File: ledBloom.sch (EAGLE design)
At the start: 4 parts, among them J1 455-1750-1-ND, J2 455-1750-1-ND, U1 WS2812

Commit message: adding production files
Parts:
- removed U1: WS2812, SparkFun-LED:WS2812"
- added D1: WS2812B, SparkFun-LED:WS2812B
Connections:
- net DI: now also D1.DI; no longer U1.DI
- net DO: now also D1.DO; no longer U1.DO
- net GND: now also D1.VSS; no longer U1.VSS
- net VCC: now also D1.VDD; no longer U1.VDD
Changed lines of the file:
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@@
 <?xml version="1.0" encoding="utf-8"?>
 <!DOCTYPE eagle SYSTEM "eagle.dtd">
-<eagle version="7.7.0">
+<eagle version="8.7.0">
 <drawing>
 <settings>
 <setting alwaysvectorfont="no"/>
+<setting keepoldvectorfont="yes"/>
 <setting verticaltext="up"/>
 </settings>
@@
 </classes>
 <parts>
-<part name="U1" library="SparkFun-LED" deviceset="WS2812" device="&quot;" value="WS2812"/>
 <part name="C1" library="SparkFun-Capacitors" deviceset="0.1UF" device="-0603-25V-(+80/-20%)" value="0.1uF"/>
 <part name="J1" library="SparkFun-Connectors" deviceset="CONN_03" device="" value="455-1750-1-ND"/>
@@
 <part name="GND3" library="SparkFun-PowerSymbols" deviceset="GND" device=""/>
 <part name="GND4" library="SparkFun-PowerSymbols" deviceset="GND" device=""/>
+<part name="D1" library="SparkFun-LED" deviceset="WS2812B" device="" value="WS2812B"/>
 </parts>
 <sheets>
@@
 </plain>
 <instances>
-<instance part="U1" gate="U1" x="43.18" y="68.58"/>
 <instance part="C1" gate="G$1" x="-2.54" y="68.58"/>
 <instance part="J1" gate="J$1" x="27.94" y="45.72" rot="R180"/>
@@
 <instance part="GND3" gate="1" x="73.66" y="33.02"/>
 <instance part="GND4" gate="1" x="10.16" y="33.02"/>
+<instance part="D1" gate="G$1" x="43.18" y="68.58"/>
 </instances>
 <busses>
@@
 <net name="DO" class="0">
 <segment>
-<pinref part="U1" gate="U1" pin="DO"/>
 <wire x1="55.88" y1="66.04" x2="60.96" y2="66.04" width="0.1524" layer="91"/>
 <label x="60.96" y="66.04" size="1.27" layer="95" xref="yes"/>
+<pinref part="D1" gate="G$1" pin="DO"/>
 </segment>
 <segment>
@@
 <net name="DI" class="0">
 <segment>
-<pinref part="U1" gate="U1" pin="DI"/>
 <wire x1="27.94" y1="66.04" x2="20.32" y2="66.04" width="0.1524" layer="91"/>
 <label x="20.32" y="66.04" size="1.27" layer="95" rot="R180" xref="yes"/>
+<pinref part="D1" gate="G$1" pin="DI"/>
 </segment>
 <segment>
@@
 </segment>
 <segment>
-<pinref part="U1" gate="U1" pin="VDD"/>
 <wire x1="27.94" y1="73.66" x2="20.32" y2="73.66" width="0.1524" layer="91"/>
 <wire x1="20.32" y1="73.66" x2="20.32" y2="78.74" width="0.1524" layer="91"/>
 <pinref part="SUPPLY3" gate="G$1" pin="VCC"/>
+<pinref part="D1" gate="G$1" pin="VDD"/>
 </segment>
 <segment>
@@
 <net name="GND" class="0">
 <segment>
-<pinref part="U1" gate="U1" pin="VSS"/>
 <wire x1="55.88" y1="73.66" x2="73.66" y2="73.66" width="0.1524" layer="91"/>
 <wire x1="73.66" y1="73.66" x2="73.66" y2="66.04" width="0.1524" layer="91"/>
 <pinref part="GND2" gate="1" pin="GND"/>
-</segment>
-<segment>
+<pinref part="D1" gate="G$1" pin="VSS"/>
+</segment>
+<segment>

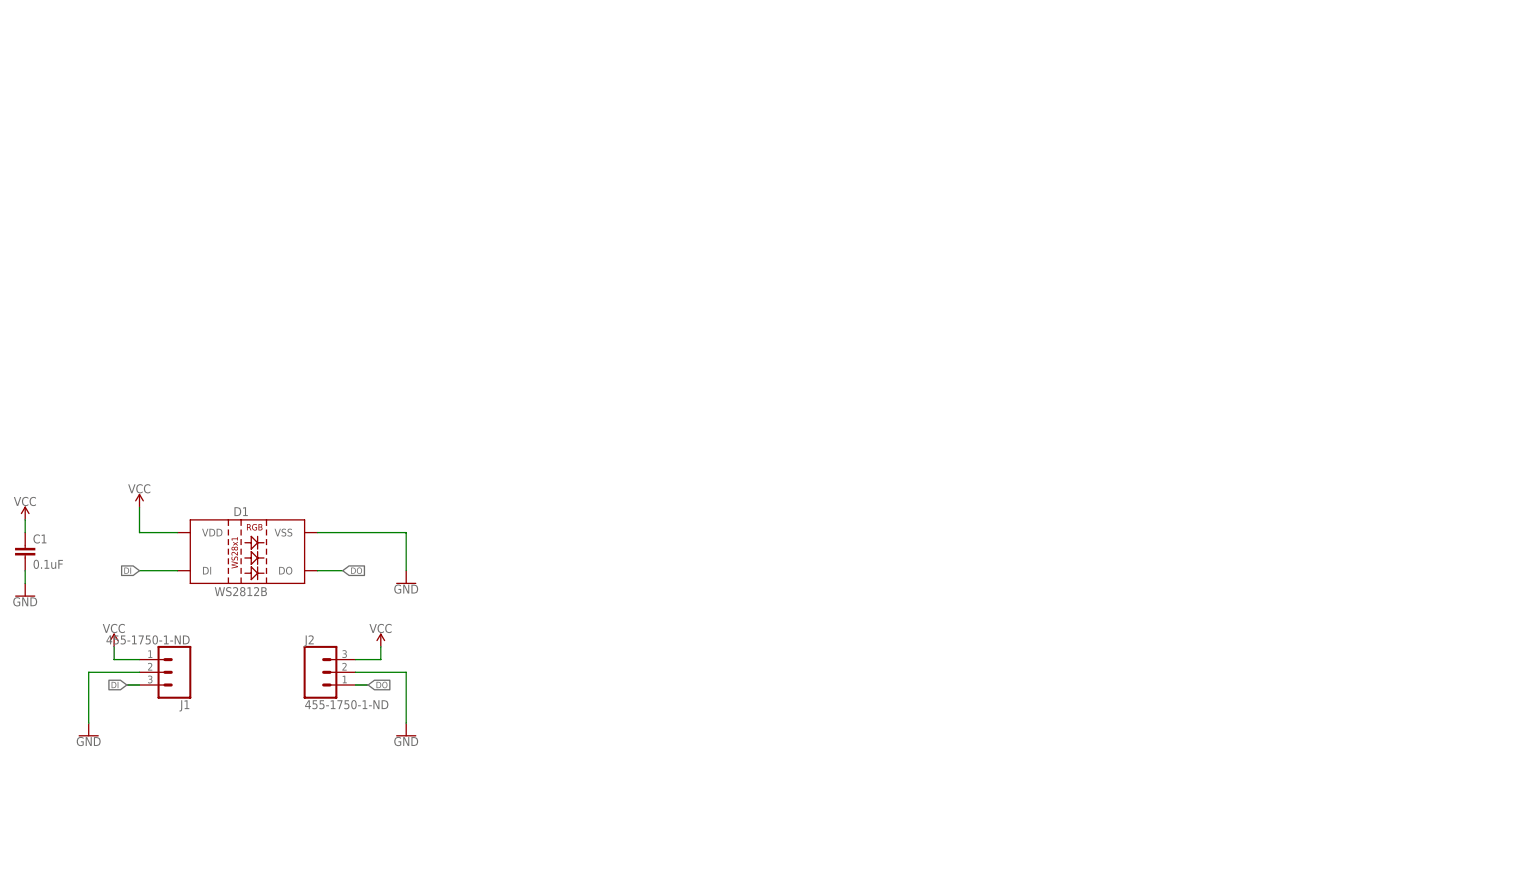
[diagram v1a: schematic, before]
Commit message: Updating Silk, adding Desert Bloom to Sch
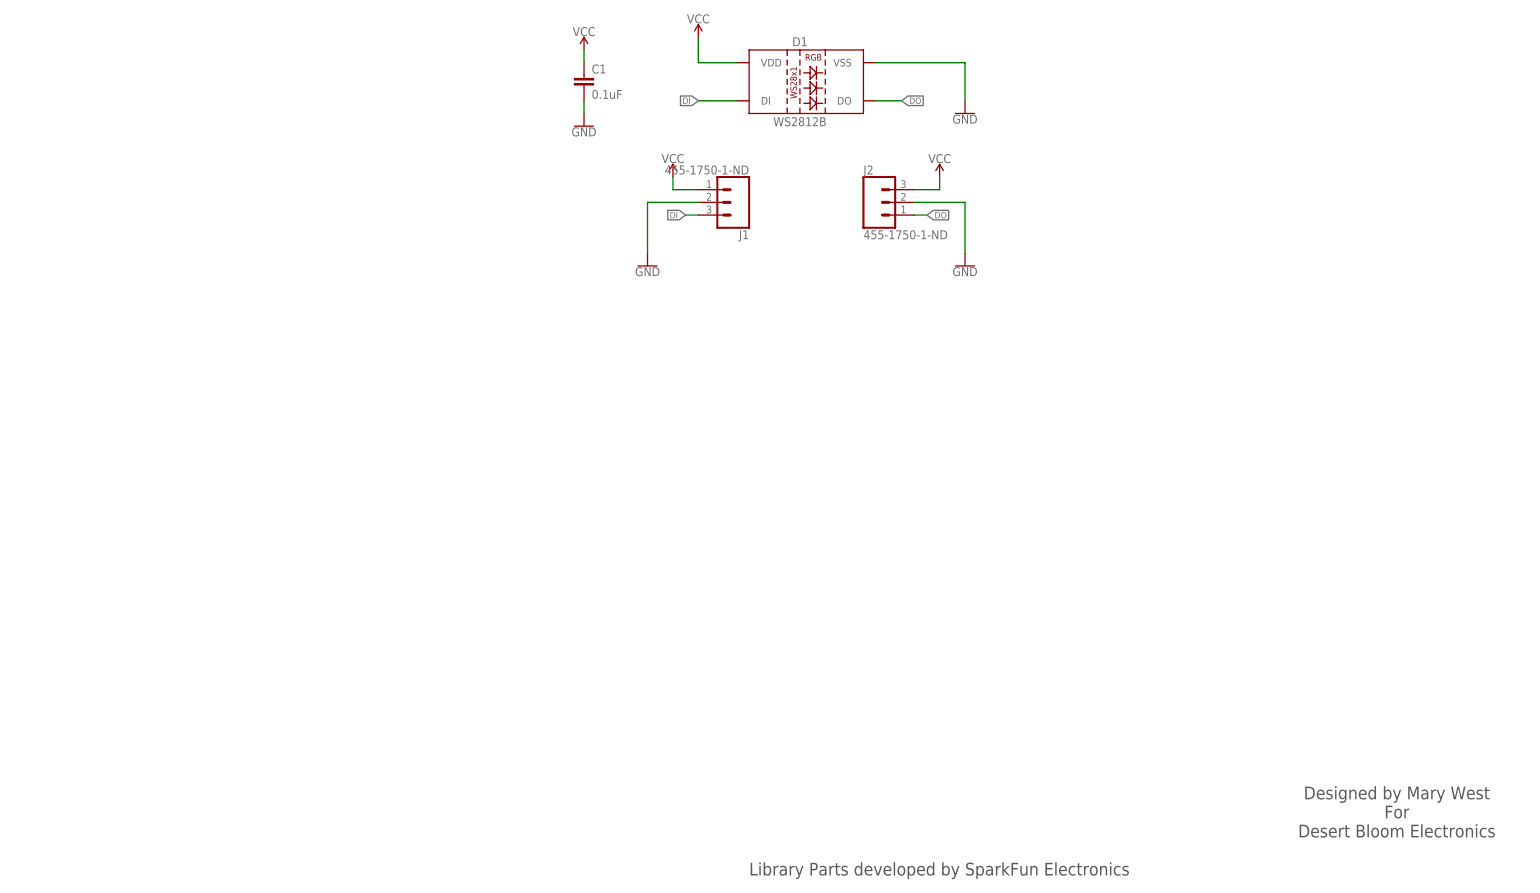
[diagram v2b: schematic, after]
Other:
- note added: "Designed by Mary West For Desert Bloom Electronics"
- note added: "Library Parts developed by SparkFun Electronics"
- moved on the sheet: C1, D1, J1, J2
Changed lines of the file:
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@@
 <part name="GND4" library="SparkFun-PowerSymbols" deviceset="GND" device=""/>
 <part name="D1" library="SparkFun-LED" deviceset="WS2812B" device="" value="WS2812B"/>
+<part name="FRAME1" library="frames" library_urn="urn:adsk.eagle:library:229" deviceset="A3L-LOC" device=""/>
 </parts>
 <sheets>
 <sheet>
 <plain>
+<text x="271.78" y="17.78" size="2.54" layer="97" font="vector" align="center">Designed by Mary West
+For
+Desert Bloom Electronics</text>
+<text x="142.24" y="5.08" size="2.54" layer="97" font="vector">Library Parts developed by SparkFun Electronics</text>
 </plain>
 <instances>
-<instance part="C1" gate="G$1" x="-2.54" y="68.58"/>
-<instance part="J1" gate="J$1" x="27.94" y="45.72" rot="R180"/>
-<instance part="J2" gate="J$1" x="55.88" y="45.72"/>
-<instance part="SUPPLY1" gate="G$1" x="15.24" y="50.8"/>
-<instance part="SUPPLY2" gate="G$1" x="68.58" y="50.8"/>
-<instance part="SUPPLY3" gate="G$1" x="20.32" y="78.74"/>
-<instance part="SUPPLY4" gate="G$1" x="-2.54" y="76.2"/>
-<instance part="GND1" gate="1" x="-2.54" y="60.96"/>
-<instance part="GND2" gate="1" x="73.66" y="63.5"/>
-<instance part="GND3" gate="1" x="73.66" y="33.02"/>
-<instance part="GND4" gate="1" x="10.16" y="33.02"/>
-<instance part="D1" gate="G$1" x="43.18" y="68.58"/>
+<instance part="C1" gate="G$1" x="109.22" y="162.56"/>
+<instance part="J1" gate="J$1" x="139.7" y="139.7" rot="R180"/>
+<instance part="J2" gate="J$1" x="167.64" y="139.7"/>
+<instance part="SUPPLY1" gate="G$1" x="127" y="144.78"/>
+<instance part="SUPPLY2" gate="G$1" x="180.34" y="144.78"/>
+<instance part="SUPPLY3" gate="G$1" x="132.08" y="172.72"/>
+<instance part="SUPPLY4" gate="G$1" x="109.22" y="170.18"/>
+<instance part="GND1" gate="1" x="109.22" y="154.94"/>
+<instance part="GND2" gate="1" x="185.42" y="157.48"/>
+<instance part="GND3" gate="1" x="185.42" y="127"/>
+<instance part="GND4" gate="1" x="121.92" y="127"/>
+<instance part="D1" gate="G$1" x="154.94" y="162.56"/>
+<instance part="FRAME1" gate="G$1" x="-43.18" y="0"/>
 </instances>
 <busses>
@@
 <net name="DO" class="0">
 <segment>
-<wire x1="55.88" y1="66.04" x2="60.96" y2="66.04" width="0.1524" layer="91"/>
-<label x="60.96" y="66.04" size="1.27" layer="95" xref="yes"/>
+<wire x1="167.64" y1="160.02" x2="172.72" y2="160.02" width="0.1524" layer="91"/>
+<label x="172.72" y="160.02" size="1.27" layer="95" xref="yes"/>
 <pinref part="D1" gate="G$1" pin="DO"/>
 </segment>
 <segment>
 <pinref part="J2" gate="J$1" pin="1"/>
-<wire x1="63.5" y1="43.18" x2="66.04" y2="43.18" width="0.1524" layer="91"/>
-<label x="66.04" y="43.18" size="1.27" layer="95" xref="yes"/>
+<wire x1="175.26" y1="137.16" x2="177.8" y2="137.16" width="0.1524" layer="91"/>
+<label x="177.8" y="137.16" size="1.27" layer="95" xref="yes"/>
 </segment>
 </net>
 <net name="DI" class="0">
 <segment>
-<wire x1="27.94" y1="66.04" x2="20.32" y2="66.04" width="0.1524" layer="91"/>
-<label x="20.32" y="66.04" size="1.27" layer="95" rot="R180" xref="yes"/>
+<wire x1="139.7" y1="160.02" x2="132.08" y2="160.02" width="0.1524" layer="91"/>
+<label x="132.08" y="160.02" size="1.27" layer="95" rot="R180" xref="yes"/>
 <pinref part="D1" gate="G$1" pin="DI"/>
 </segment>
 <segment>
 <pinref part="J1" gate="J$1" pin="3"/>
-<wire x1="20.32" y1="43.18" x2="17.78" y2="43.18" width="0.1524" layer="91"/>
-<label x="17.78" y="43.18" size="1.27" layer="95" rot="R180" xref="yes"/>
+<wire x1="132.08" y1="137.16" x2="129.54" y2="137.16" width="0.1524" layer="91"/>
+<label x="129.54" y="137.16" size="1.27" layer="95" rot="R180" xref="yes"/>
 </segment>
 </net>
@@
 <segment>
 <pinref part="J1" gate="J$1" pin="1"/>
-<wire x1="20.32" y1="48.26" x2="15.24" y2="48.26" width="0.1524" layer="91"/>
-<wire x1="15.24" y1="48.26" x2="15.24" y2="50.8" width="0.1524" layer="91"/>
+<wire x1="132.08" y1="142.24" x2="127" y2="142.24" width="0.1524" layer="91"/>
+<wire x1="127" y1="142.24" x2="127" y2="144.78" width="0.1524" layer="91"/>
 <pinref part="SUPPLY1" gate="G$1" pin="VCC"/>
 </segment>
 <segment>
 <pinref part="J2" gate="J$1" pin="3"/>
-<wire x1="63.5" y1="48.26" x2="68.58" y2="48.26" width="0.1524" layer="91"/>
-<wire x1="68.58" y1="48.26" x2="68.58" y2="50.8" width="0.1524" layer="91"/>
+<wire x1="175.26" y1="142.24" x2="180.34" y2="142.24" width="0.1524" layer="91"/>
+<wire x1="180.34" y1="142.24" x2="180.34" y2="144.78" width="0.1524" layer="91"/>
 <pinref part="SUPPLY2" gate="G$1" pin="VCC"/>
 </segment>
 <segment>
-<wire x1="27.94" y1="73.66" x2="20.32" y2="73.66" width="0.1524" layer="91"/>
-<wire x1="20.32" y1="73.66" x2="20.32" y2="78.74" width="0.1524" layer="91"/>
+<wire x1="139.7" y1="167.64" x2="132.08" y2="167.64" width="0.1524" layer="91"/>
+<wire x1="132.08" y1="167.64" x2="132.08" y2="172.72" width="0.1524" layer="91"/>
 <pinref part="SUPPLY3" gate="G$1" pin="VCC"/>
 <pinref part="D1" gate="G$1" pin="VDD"/>
@@
 <pinref part="C1" gate="G$1" pin="1"/>
 <pinref part="SUPPLY4" gate="G$1" pin="VCC"/>
-<wire x1="-2.54" y1="73.66" x2="-2.54" y2="76.2" width="0.1524" layer="91"/>
+<wire x1="109.22" y1="167.64" x2="109.22" y2="170.18" width="0.1524" layer="91"/>
 </segment>
 </net>
 <net name="GND" class="0">
 <segment>
-<wire x1="55.88" y1="73.66" x2="73.66" y2="73.66" width="0.1524" layer="91"/>
-<wire x1="73.66" y1="73.66" x2="73.66" y2="66.04" width="0.1524" layer="91"/>
+<wire x1="167.64" y1="167.64" x2="185.42" y2="167.64" width="0.1524" layer="91"/>
+<wire x1="185.42" y1="167.64" x2="185.42" y2="160.02" width="0.1524" layer="91"/>
 <pinref part="GND2" gate="1" pin="GND"/>
 <pinref part="D1" gate="G$1" pin="VSS"/>
@@
 <segment>
 <pinref part="J2" gate="J$1" pin="2"/>
-<wire x1="63.5" y1="45.72" x2="73.66" y2="45.72" width="0.1524" layer="91"/>
-<wire x1="73.66" y1="45.72" x2="73.66" y2="35.56" width="0.1524" layer="91"/>
+<wire x1="175.26" y1="139.7" x2="185.42" y2="139.7" width="0.1524" layer="91"/>
+<wire x1="185.42" y1="139.7" x2="185.42" y2="129.54" width="0.1524" layer="91"/>
 <pinref part="GND3" gate="1" pin="GND"/>
 </segment>
 <segment>
 <pinref part="J1" gate="J$1" pin="2"/>
-<wire x1="20.32" y1="45.72" x2="10.16" y2="45.72" width="0.1524" layer="91"/>
-<wire x1="10.16" y1="45.72" x2="10.16" y2="35.56" width="0.1524" layer="91"/>
+<wire x1="132.08" y1="139.7" x2="121.92" y2="139.7" width="0.1524" layer="91"/>
+<wire x1="121.92" y1="139.7" x2="121.92" y2="129.54" width="0.1524" layer="91"/>
 <pinref part="GND4" gate="1" pin="GND"/>
 </segment>
@@
 <pinref part="GND1" gate="1" pin="GND"/>
 <pinref part="C1" gate="G$1" pin="2"/>
-<wire x1="-2.54" y1="63.5" x2="-2.54" y2="66.04" width="0.1524" layer="91"/>
+<wire x1="109.22" y1="157.48" x2="109.22" y2="160.02" width="0.1524" layer="91"/>
 </segment>
 </net>
@@
 </schematic>
 </drawing>
+<compatibility>
+<note version="6.3" minversion="6.2.2" severity="warning">
+Since Version 6.2.2 text objects can contain more than one line,
+which will not be processed correctly with this version.
+</note>
+<note version="8.2" severity="warning">
+Since Version 8.2, EAGLE supports online libraries. The ids
+of those online libraries will not be understood (or retained)
+with this version.
+</note>
+<note version="8.3" severity="warning">
+Since Version 8.3, EAGLE supports URNs for individual library
+assets (packages, symbols, and devices). The URNs of those assets
+will not be understood (or retained) with this version.
+</note>
+</compatibility>
 </eagle>
